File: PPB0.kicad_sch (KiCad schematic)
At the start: 8 parts, among them U6 74LS08

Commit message: Added first set of condensing adders, down to 4 rows total of Partials to add
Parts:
- renumbered C to C5, U to U7
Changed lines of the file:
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@@
 		(dnp no)
 		(fields_autoplaced yes)
-		(property "Reference" "U"
+		(property "Reference" "U?"
 			(at 93.98 41.9182 90)
 			(effects
@@
 				(path "/a3259cd8-3487-4a9b-97aa-d93f94f5405f/bf82ace6-846a-4d9d-a653-74fa3e3ba646/2c703ca2-04cd-4721-ae83-f8263d8cee5a"
 					(reference "U15")
+					(unit 1)
+				)
+				(path "/a3259cd8-3487-4a9b-97aa-d93f94f5405f/bf82ace6-846a-4d9d-a653-74fa3e3ba646/4384cd5f-bb64-4e11-ba13-ffbedd074d3b"
+					(reference "U?")
 					(unit 1)
 				)
@@
 		(dnp no)
 		(fields_autoplaced yes)
-		(property "Reference" "#PWR"
+		(property "Reference" "#PWR?"
 			(at 222.25 67.31 0)
 			(effects
@@
 				(path "/a3259cd8-3487-4a9b-97aa-d93f94f5405f/bf82ace6-846a-4d9d-a653-74fa3e3ba646/2c703ca2-04cd-4721-ae83-f8263d8cee5a"
 					(reference "#PWR076")
+					(unit 1)
+				)
+				(path "/a3259cd8-3487-4a9b-97aa-d93f94f5405f/bf82ace6-846a-4d9d-a653-74fa3e3ba646/4384cd5f-bb64-4e11-ba13-ffbedd074d3b"
+					(reference "#PWR?")
 					(unit 1)
 				)
@@
 		(dnp no)
 		(fields_autoplaced yes)
-		(property "Reference" "#PWR"
+		(property "Reference" "#PWR?"
 			(at 191.77 52.07 0)
 			(effects
@@
 				(path "/a3259cd8-3487-4a9b-97aa-d93f94f5405f/bf82ace6-846a-4d9d-a653-74fa3e3ba646/2c703ca2-04cd-4721-ae83-f8263d8cee5a"
 					(reference "#PWR070")
+					(unit 1)
+				)
+				(path "/a3259cd8-3487-4a9b-97aa-d93f94f5405f/bf82ace6-846a-4d9d-a653-74fa3e3ba646/4384cd5f-bb64-4e11-ba13-ffbedd074d3b"
+					(reference "#PWR?")
 					(unit 1)
 				)
@@
 		(dnp no)
 		(fields_autoplaced yes)
-		(property "Reference" "#PWR"
+		(property "Reference" "#PWR?"
 			(at 222.25 43.18 0)
 			(effects
@@
 				(path "/a3259cd8-3487-4a9b-97aa-d93f94f5405f/bf82ace6-846a-4d9d-a653-74fa3e3ba646/2c703ca2-04cd-4721-ae83-f8263d8cee5a"
 					(reference "#PWR075")
+					(unit 1)
+				)
+				(path "/a3259cd8-3487-4a9b-97aa-d93f94f5405f/bf82ace6-846a-4d9d-a653-74fa3e3ba646/4384cd5f-bb64-4e11-ba13-ffbedd074d3b"
+					(reference "#PWR?")
 					(unit 1)
 				)
@@
 		(on_board yes)
 		(dnp no)
-		(property "Reference" "U"
+		(property "Reference" "U?"
 			(at 160.02 41.9182 90)
 			(effects
@@
 					(reference "U15")
 					(unit 4)
+				)
+				(path "/a3259cd8-3487-4a9b-97aa-d93f94f5405f/bf82ace6-846a-4d9d-a653-74fa3e3ba646/4384cd5f-bb64-4e11-ba13-ffbedd074d3b"
+					(reference "U?")
+					(unit 1)
 				)
 				(path "/a3259cd8-3487-4a9b-97aa-d93f94f5405f/bf82ace6-846a-4d9d-a653-74fa3e3ba646/4af9546c-6036-47f2-8410-f9b2b134253c"
@@
 		(dnp no)
 		(fields_autoplaced yes)
-		(property "Reference" "#PWR"
+		(property "Reference" "#PWR?"
 			(at 194.31 43.18 0)
 			(effects
@@
 				(path "/a3259cd8-3487-4a9b-97aa-d93f94f5405f/bf82ace6-846a-4d9d-a653-74fa3e3ba646/2c703ca2-04cd-4721-ae83-f8263d8cee5a"
 					(reference "#PWR071")
+					(unit 1)
+				)
+				(path "/a3259cd8-3487-4a9b-97aa-d93f94f5405f/bf82ace6-846a-4d9d-a653-74fa3e3ba646/4384cd5f-bb64-4e11-ba13-ffbedd074d3b"
+					(reference "#PWR?")
 					(unit 1)
 				)
@@
 		(on_board yes)
 		(dnp no)
-		(property "Reference" "C"
+		(property "Reference" "C?"
 			(at 190.5 79.756 90)
 			(effects
@@
 				(path "/a3259cd8-3487-4a9b-97aa-d93f94f5405f/bf82ace6-846a-4d9d-a653-74fa3e3ba646/2c703ca2-04cd-4721-ae83-f8263d8cee5a"
 					(reference "C13")
+					(unit 1)
+				)
+				(path "/a3259cd8-3487-4a9b-97aa-d93f94f5405f/bf82ace6-846a-4d9d-a653-74fa3e3ba646/4384cd5f-bb64-4e11-ba13-ffbedd074d3b"
+					(reference "C?")
 					(unit 1)
 				)
@@
 		(dnp no)
 		(fields_autoplaced yes)
-		(property "Reference" "U"
+		(property "Reference" "U?"
 			(at 137.16 41.9182 90)
 			(effects
@@
 					(reference "U15")
 					(unit 3)
+				)
+				(path "/a3259cd8-3487-4a9b-97aa-d93f94f5405f/bf82ace6-846a-4d9d-a653-74fa3e3ba646/4384cd5f-bb64-4e11-ba13-ffbedd074d3b"
+					(reference "U?")
+					(unit 1)
 				)
 				(path "/a3259cd8-3487-4a9b-97aa-d93f94f5405f/bf82ace6-846a-4d9d-a653-74fa3e3ba646/4af9546c-6036-47f2-8410-f9b2b134253c"
@@
 		(dnp no)
 		(fields_autoplaced yes)
-		(property "Reference" "U"
+		(property "Reference" "U?"
 			(at 115.57 41.9182 90)
 			(effects
@@
 					(reference "U15")
 					(unit 2)
+				)
+				(path "/a3259cd8-3487-4a9b-97aa-d93f94f5405f/bf82ace6-846a-4d9d-a653-74fa3e3ba646/4384cd5f-bb64-4e11-ba13-ffbedd074d3b"
+					(reference "U?")
+					(unit 1)
 				)
 				(path "/a3259cd8-3487-4a9b-97aa-d93f94f5405f/bf82ace6-846a-4d9d-a653-74fa3e3ba646/4af9546c-6036-47f2-8410-f9b2b134253c"
@@
 		(dnp no)
 		(fields_autoplaced yes)
-		(property "Reference" "U"
+		(property "Reference" "U?"
 			(at 203.2 33.02 90)
 			(effects
@@
 					(unit 5)
 				)
+				(path "/a3259cd8-3487-4a9b-97aa-d93f94f5405f/bf82ace6-846a-4d9d-a653-74fa3e3ba646/4384cd5f-bb64-4e11-ba13-ffbedd074d3b"
+					(reference "U?")
+					(unit 1)
+				)
 				(path "/a3259cd8-3487-4a9b-97aa-d93f94f5405f/bf82ace6-846a-4d9d-a653-74fa3e3ba646/4af9546c-6036-47f2-8410-f9b2b134253c"

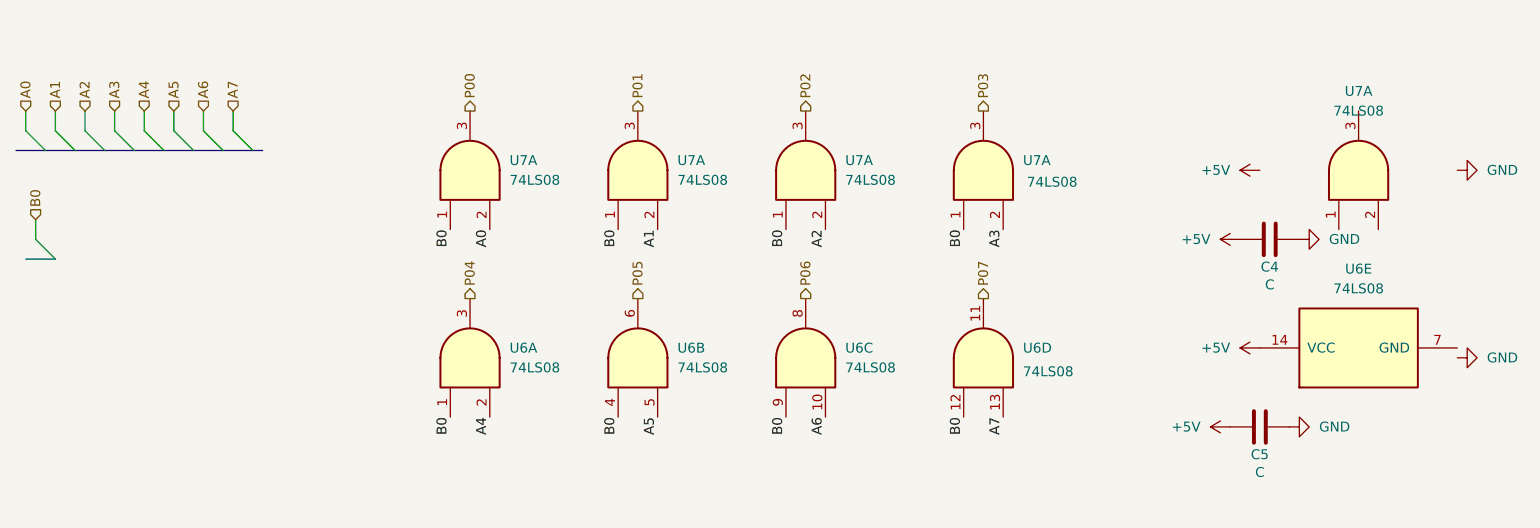
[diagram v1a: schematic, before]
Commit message: Fixed ERC issues and applied Footprints
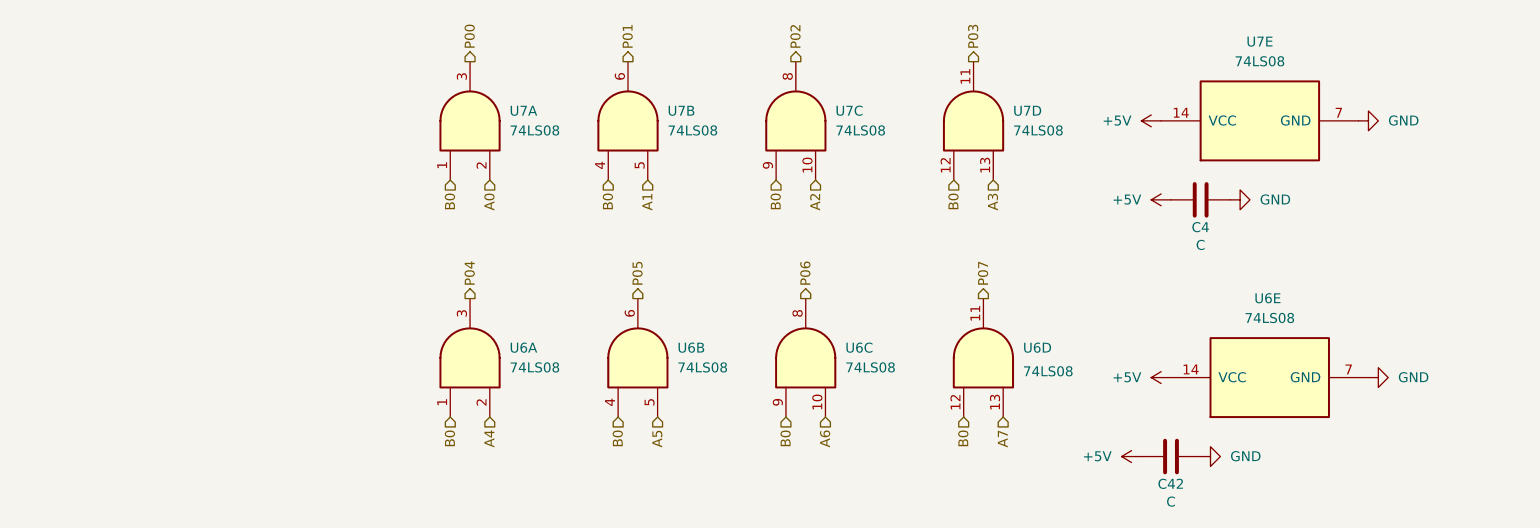
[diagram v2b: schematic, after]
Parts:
- removed U7 (x5): 74LS08, symbol 74xx:74LS08
- added U7: 74LS08, Package_SO:SOIC-14-16_3.9x9.9mm_P1.27mm, symbol 74xx:74LS08
- C4: footprint (none) -> Capacitor_SMD:C_0402_1005Metric
- C42: renamed from C5; footprint (none) -> Capacitor_SMD:C_0402_1005Metric
- U6: footprint (none) -> Package_SO:SOIC-14-16_3.9x9.9mm_P1.27mm
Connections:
- net +5V: now also U7.14 (VCC)
- net A0: now also U7.2
- net A1: now also U7.5
- net A2: now also U7.10
- net A3: now also U7.13
- net B0: now also U7.1, U7.12, U7.4, U7.9
- net GND: now also U6.7 (GND), U7.7 (GND)
- net P00: now also U7.3
- net P01: now also U7.6
- net P02: now also U7.8
- net P03: now also U7.11
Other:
- moved on the sheet: C4, C42, U6E
